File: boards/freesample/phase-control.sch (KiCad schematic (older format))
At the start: 18 parts, among them U16 HMC856, U17 NB6L295

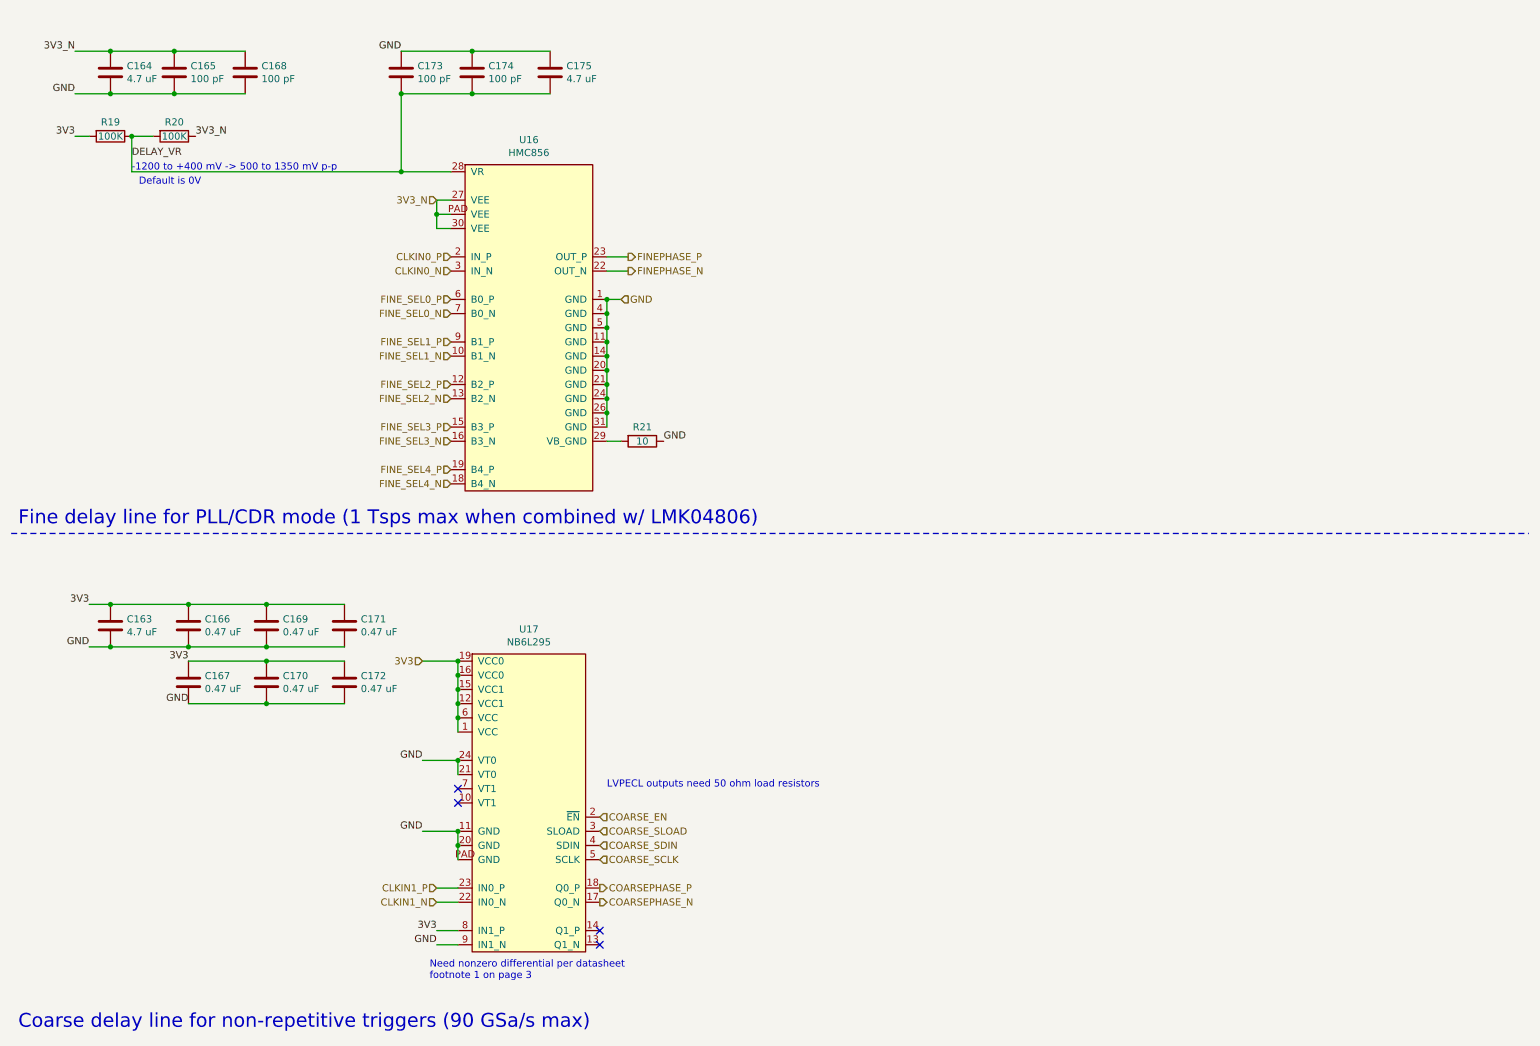
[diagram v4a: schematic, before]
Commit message: Continued schematic capture work. Hooked up most SoM connectors.
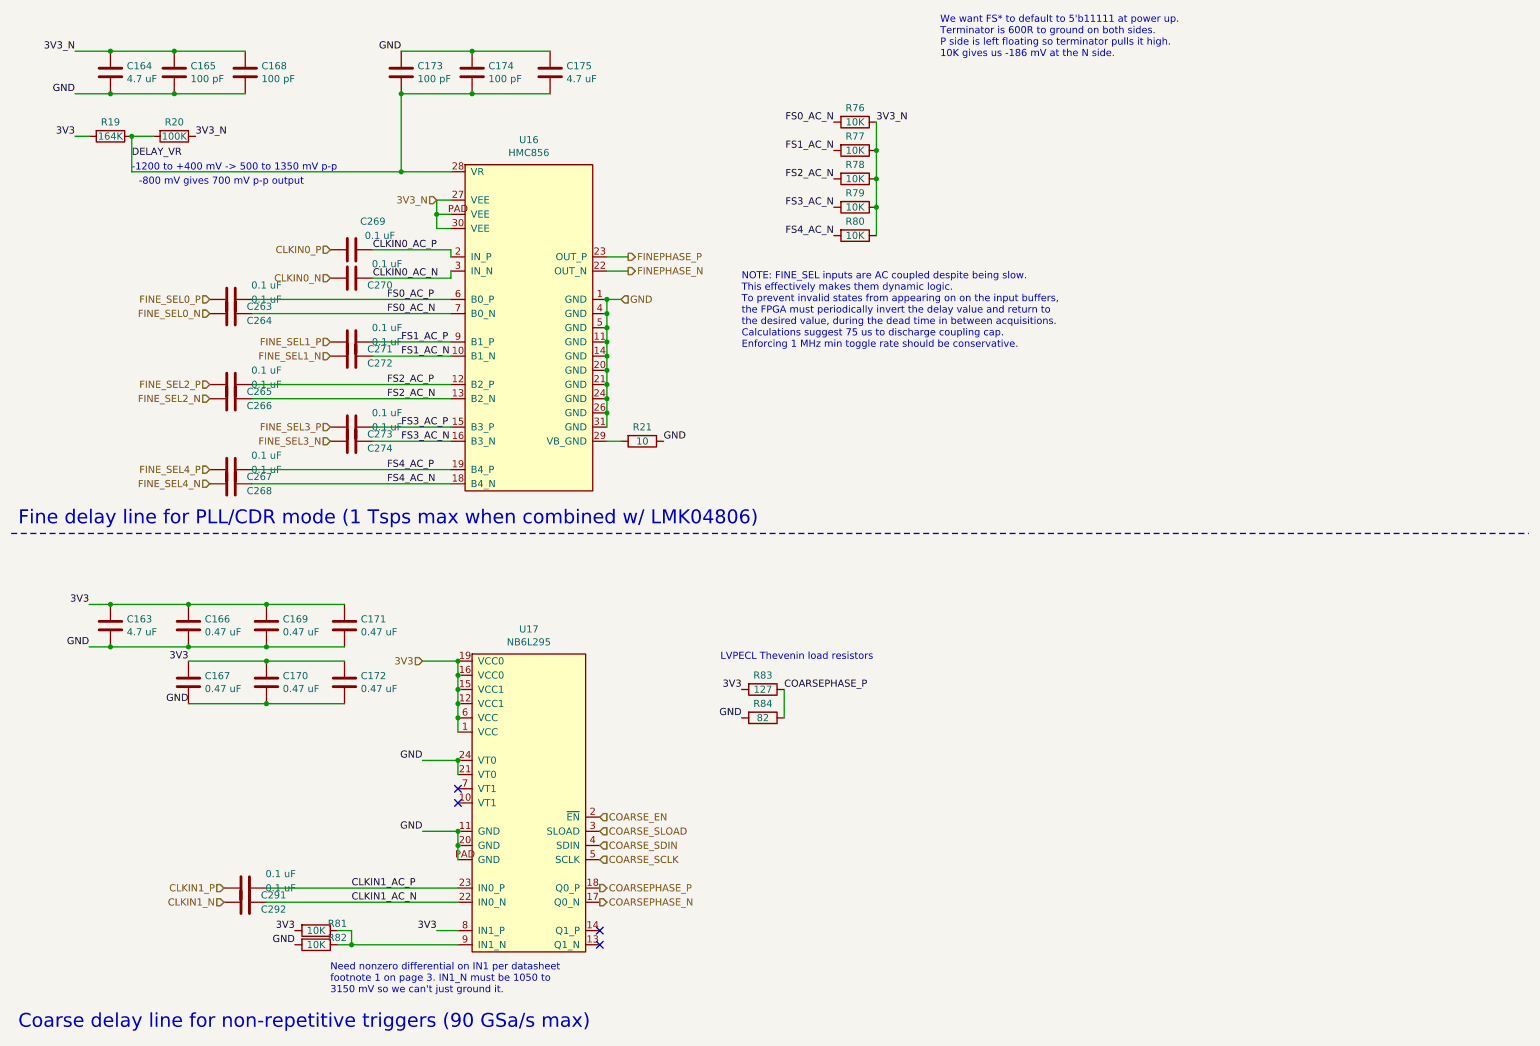
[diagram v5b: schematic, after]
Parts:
- added C263, C264, C265, C266, C267, C268, C269, C270, C271, C272, C273, C274, C291, C292: 0.1 uF, symbol device:C
- added R76, R77, R78, R79, R80, R81, R82: 10K, symbol device:R
- added R83: 127, symbol device:R
- added R84: 82, symbol device:R
- R19: value 100K -> 164K
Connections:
- net 3V3: now also R81.2, R83.2
- net 3V3_N: now also R76.1, R77.1, R78.1, R79.1, R80.1
- net CLKIN0_N: now also C270.2; no longer U16.3 (IN_N)
- net CLKIN0_P: now also C269.2; no longer U16.2 (IN_P)
- net CLKIN1_N: now also C292.2; no longer U17.22 (IN0_N)
- net CLKIN1_P: now also C291.2; no longer U17.23 (IN0_P)
- net COARSEPHASE_P: now also R83.1, R84.1
- net FINE_SEL0_N: now also C264.2; no longer U16.7 (B0_N)
- net FINE_SEL0_P: now also C263.2; no longer U16.6 (B0_P)
- net FINE_SEL1_N: now also C272.2; no longer U16.10 (B1_N)
- net FINE_SEL1_P: now also C271.2; no longer U16.9 (B1_P)
- net FINE_SEL2_N: now also C266.2; no longer U16.13 (B2_N)
- net FINE_SEL2_P: now also C265.2; no longer U16.12 (B2_P)
- net FINE_SEL3_N: now also C274.2; no longer U16.16 (B3_N)
- net FINE_SEL3_P: now also C273.2; no longer U16.15 (B3_P)
- net FINE_SEL4_N: now also C268.2; no longer U16.18 (B4_N)
- net FINE_SEL4_P: now also C267.2; no longer U16.19 (B4_P)
- net GND: now also R82.2, R84.2; no longer U17.9 (IN1_N)
- new net: R81.1, R82.1, U17.9 (IN1_N)
- new net CLKIN0_AC_N: C270.1, U16.3 (IN_N)
- new net CLKIN0_AC_P: C269.1, U16.2 (IN_P)
- new net CLKIN1_AC_N: C292.1, U17.22 (IN0_N)
- new net CLKIN1_AC_P: C291.1, U17.23 (IN0_P)
- new net FS0_AC_N: C264.1, R76.2, U16.7 (B0_N)
- new net FS0_AC_P: C263.1, U16.6 (B0_P)
- new net FS1_AC_N: C272.1, R77.2, U16.10 (B1_N)
- new net FS1_AC_P: C271.1, U16.9 (B1_P)
- new net FS2_AC_N: C266.1, R78.2, U16.13 (B2_N)
- new net FS2_AC_P: C265.1, U16.12 (B2_P)
- new net FS3_AC_N: C274.1, R79.2, U16.16 (B3_N)
- new net FS3_AC_P: C273.1, U16.15 (B3_P)
- new net FS4_AC_N: C268.1, R80.2, U16.18 (B4_N)
- new net FS4_AC_P: C267.1, U16.19 (B4_P)
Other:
- note added: "-800 mV gives 700 mV p-p output"
- note added: "LVPECL Thevenin load resistors"
- note added: "NOTE: FINE_SEL inputs are AC coupled despite being slow.\nThis effectively makes them dynamic logic.\nTo prevent invalid states from appearing on on the input buffers,\nthe FPGA must periodically invert the delay value and return to\nthe desired value, during the dead time in between acquisitions.\nCalculations suggest 75 us to discharge coupling cap.\nEnforcing 1 MHz min toggle rate should be co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"
- note added: "Need nonzero differential on IN1 per datasheet\nfootnote 1 on page 3. IN1_N must be 1050 to\n3150 mV so we can't just ground it."
- note added: "We want FS* to default to 5'b11111 at power up.\nTerminator is 600R to ground on both sides.\nP side is left floating so terminator pulls it high.\n10K gives us -186 mV at the N side."
- note removed: "Default is 0V"
- note removed: "LVPECL outputs need 50 ohm load resistors"
- note removed: "Need nonzero differential per datasheet\nfootnote 1 on page 3"

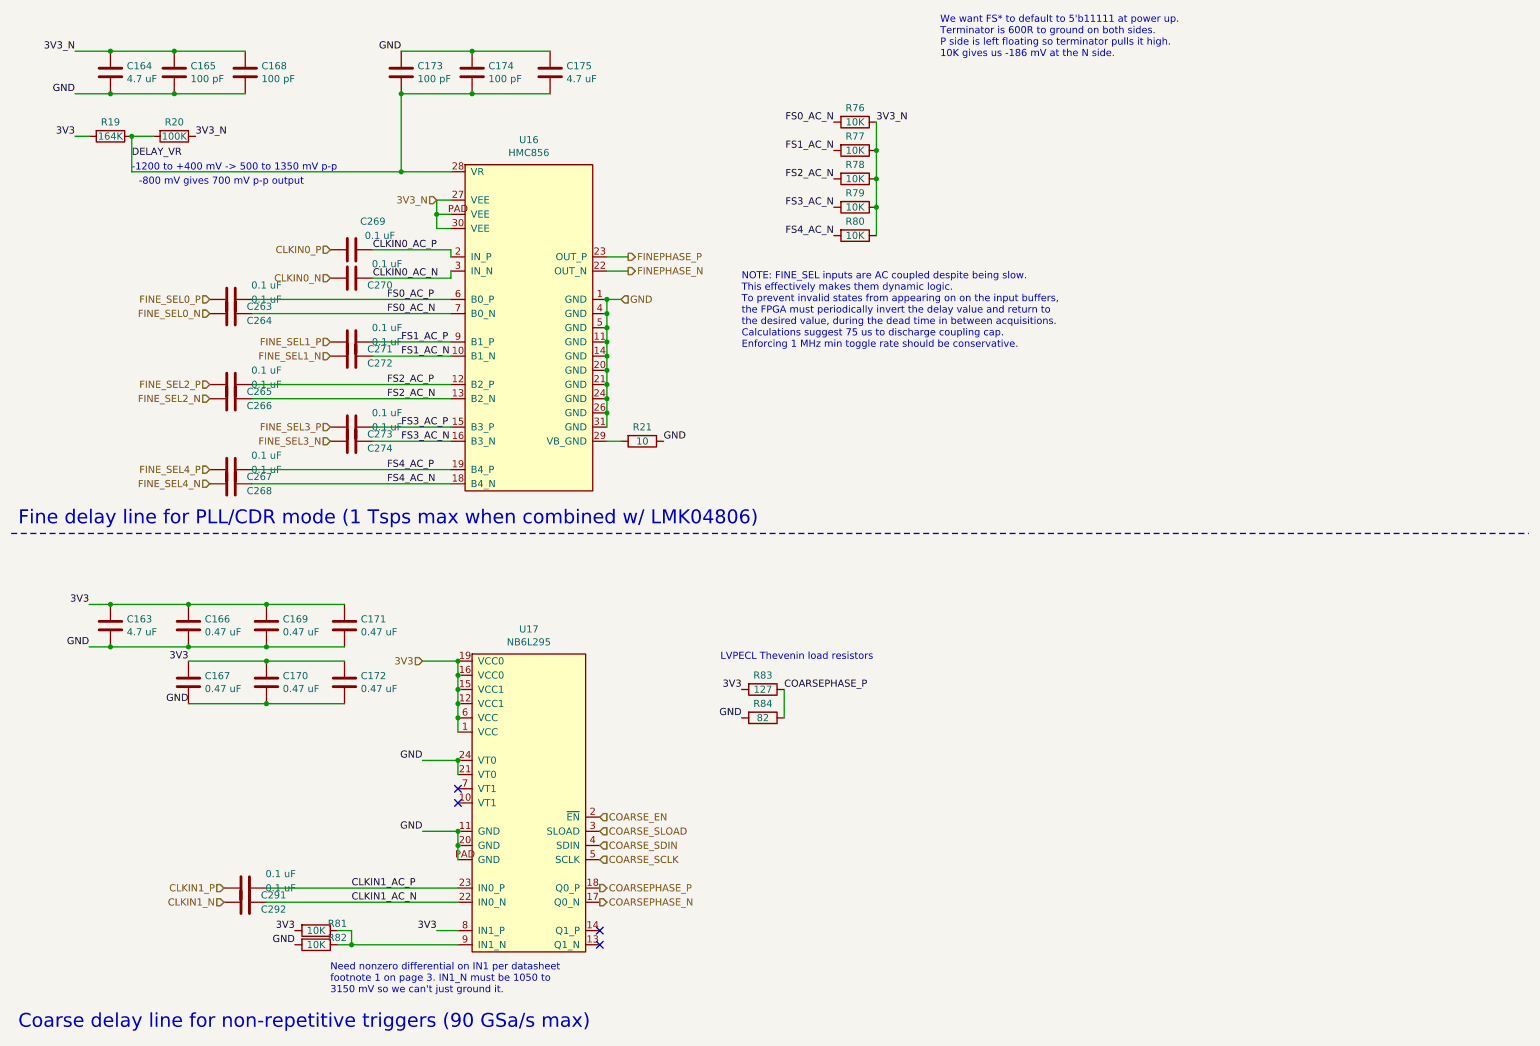
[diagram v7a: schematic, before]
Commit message: Specified part number for AC coupling caps
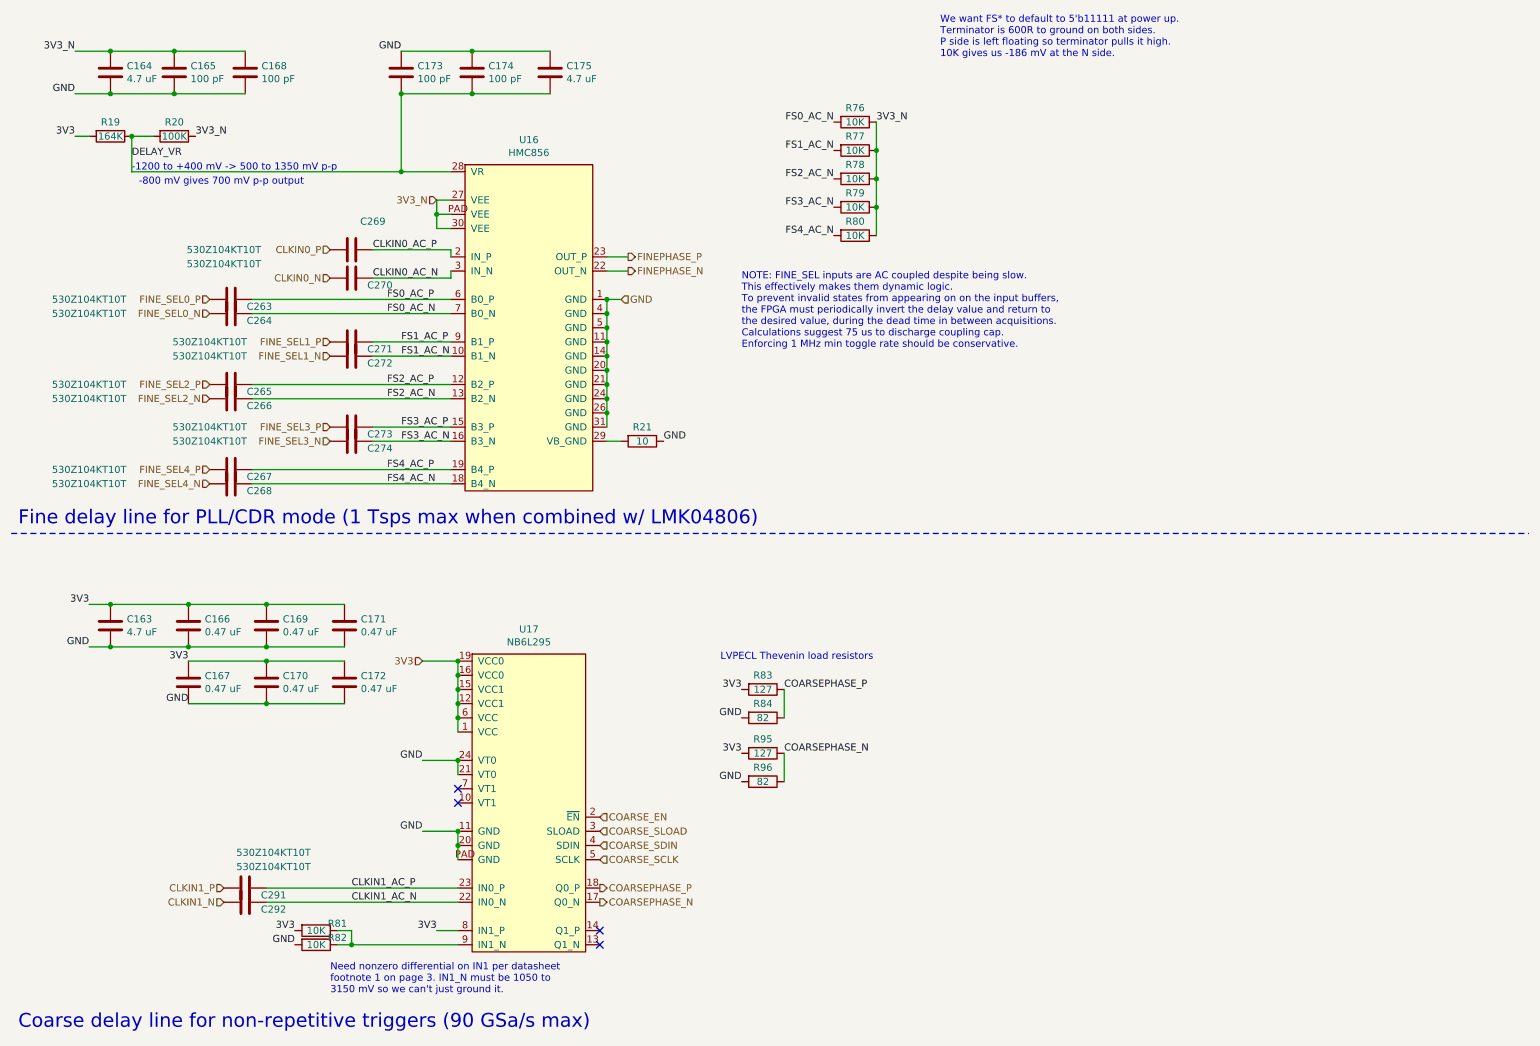
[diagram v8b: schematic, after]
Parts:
- added R95: 127, symbol device:R
- added R96: 82, symbol device:R
- C263, C264, C265, C266, C267, C268, C269, C270, C271, C272, C273, C274, C291, C292: value 0.1 uF -> 530Z104KT10T
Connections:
- net 3V3: now also R95.2
- net COARSEPHASE_N: now also R95.1, R96.1
- net GND: now also R96.2
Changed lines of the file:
@@
 Sheet 12 12
 Title "FREESAMPLE Oscilloscope"
-Date "2019-03-11"
+Date "2019-03-13"
 Rev "0.1"
 Comp "Andrew D. Zonenberg / Antikernel Labs"
@@
 P 2900 2200
 F 0 "C269" V 2700 2350 50  0000 C CNN
-F 1 "0.1 uF" V 2800 2400 50  0000 C CNN
+F 1 "530Z104KT10T" V 2900 1300 50  0000 C CNN
 F 2 "" H 2938 2050 50  0001 C CNN
 F 3 "" H 2900 2200 50  0001 C CNN
@@
 P 2900 2400
 F 0 "C270" V 2950 2600 50  0000 C CNN
-F 1 "0.1 uF" V 2800 2650 50  0000 C CNN
+F 1 "530Z104KT10T" V 2800 1500 50  0000 C CNN
 F 2 "" H 2938 2250 50  0001 C CNN
 F 3 "" H 2900 2400 50  0001 C CNN
@@
 P 2050 2550
 F 0 "C263" V 2100 2750 50  0000 C CNN
-F 1 "0.1 uF" V 1950 2800 50  0000 C CNN
+F 1 "530Z104KT10T" V 2050 1550 50  0000 C CNN
 F 2 "" H 2088 2400 50  0001 C CNN
 F 3 "" H 2050 2550 50  0001 C CNN
@@
 P 2050 2650
 F 0 "C264" V 2100 2850 50  0000 C CNN
-F 1 "0.1 uF" V 1950 2900 50  0000 C CNN
+F 1 "530Z104KT10T" V 2050 1650 50  0000 C CNN
 F 2 "" H 2088 2500 50  0001 C CNN
 F 3 "" H 2050 2650 50  0001 C CNN
@@
 P 2900 2850
 F 0 "C271" V 2950 3050 50  0000 C CNN
-F 1 "0.1 uF" V 2800 3100 50  0000 C CNN
+F 1 "530Z104KT10T" V 2900 1850 50  0000 C CNN
 F 2 "" H 2938 2700 50  0001 C CNN
 F 3 "" H 2900 2850 50  0001 C CNN
@@
 P 2900 2950
 F 0 "C272" V 2950 3150 50  0000 C CNN
-F 1 "0.1 uF" V 2800 3200 50  0000 C CNN
+F 1 "530Z104KT10T" V 2900 1950 50  0000 C CNN
 F 2 "" H 2938 2800 50  0001 C CNN
 F 3 "" H 2900 2950 50  0001 C CNN
@@
 P 2050 3150
 F 0 "C265" V 2100 3350 50  0000 C CNN
-F 1 "0.1 uF" V 1950 3400 50  0000 C CNN
+F 1 "530Z104KT10T" V 2050 2150 50  0000 C CNN
 F 2 "" H 2088 3000 50  0001 C CNN
 F 3 "" H 2050 3150 50  0001 C CNN
@@
 P 2050 3250
 F 0 "C266" V 2100 3450 50  0000 C CNN
-F 1 "0.1 uF" V 1950 3500 50  0000 C CNN
+F 1 "530Z104KT10T" V 2050 2250 50  0000 C CNN
 F 2 "" H 2088 3100 50  0001 C CNN
 F 3 "" H 2050 3250 50  0001 C CNN
@@
 P 2900 3450
 F 0 "C273" V 2950 3650 50  0000 C CNN
-F 1 "0.1 uF" V 2800 3700 50  0000 C CNN
+F 1 "530Z104KT10T" V 2900 2450 50  0000 C CNN
 F 2 "" H 2938 3300 50  0001 C CNN
 F 3 "" H 2900 3450 50  0001 C CNN
@@
 P 2900 3550
 F 0 "C274" V 2950 3750 50  0000 C CNN
-F 1 "0.1 uF" V 2800 3800 50  0000 C CNN
+F 1 "530Z104KT10T" V 2900 2550 50  0000 C CNN
 F 2 "" H 2938 3400 50  0001 C CNN
 F 3 "" H 2900 3550 50  0001 C CNN
@@
 P 2050 3750
 F 0 "C267" V 2100 3950 50  0000 C CNN
-F 1 "0.1 uF" V 1950 4000 50  0000 C CNN
+F 1 "530Z104KT10T" V 2050 2750 50  0000 C CNN
 F 2 "" H 2088 3600 50  0001 C CNN
 F 3 "" H 2050 3750 50  0001 C CNN
@@
 P 2050 3850
 F 0 "C268" V 2100 4050 50  0000 C CNN
-F 1 "0.1 uF" V 1950 4100 50  0000 C CNN
+F 1 "530Z104KT10T" V 2050 2850 50  0000 C CNN
 F 2 "" H 2088 3700 50  0001 C CNN
 F 3 "" H 2050 3850 50  0001 C CNN
@@
 P 2150 6700
 F 0 "C291" V 2200 6900 50  0000 C CNN
-F 1 "0.1 uF" V 2050 6950 50  0000 C CNN
+F 1 "530Z104KT10T" V 1900 6900 50  0000 C CNN
 F 2 "" H 2188 6550 50  0001 C CNN
 F 3 "" H 2150 6700 50  0001 C CNN
@@
 P 2150 6800
 F 0 "C292" V 2200 7000 50  0000 C CNN
-F 1 "0.1 uF" V 2050 7050 50  0000 C CNN
+F 1 "530Z104KT10T" V 1900 7000 50  0000 C CNN
 F 2 "" H 2188 6650 50  0001 C CNN
 F 3 "" H 2150 6800 50  0001 C CNN
@@
 Wire Wire Line
 	4800 3550 4700 3550
+$Comp
+L device:R R95
+U 1 1 5D419879
+P 5800 5750
+F 0 "R95" V 5700 5750 50  0000 C CNN
+F 1 "127" V 5800 5750 50  0000 C CNN
+F 2 "" V 5730 5750 50  0001 C CNN
+F 3 "" H 5800 5750 50  0001 C CNN
+	1    5800 5750
+	0    1    1    0
+$EndComp
+Text Label 5950 5750 0    50   ~ 0
+COARSEPHASE_N
+Text Label 5650 5750 2    50   ~ 0
+3V3
+$Comp
+L device:R R96
+U 1 1 5D419885
+P 5800 5950
+F 0 "R96" V 5700 5950 50  0000 C CNN
+F 1 "82" V 5800 5950 50  0000 C CNN
+F 2 "" V 5730 5950 50  0001 C CNN
+F 3 "" H 5800 5950 50  0001 C CNN
+	1    5800 5950
+	0    1    1    0
+$EndComp
+Text Label 5650 5950 2    50   ~ 0
+GND
+Wire Wire Line
+	5950 5950 5950 5750
 $EndSCHEMATC
